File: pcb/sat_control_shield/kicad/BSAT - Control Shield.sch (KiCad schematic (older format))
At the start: 11 parts, among them P1 POWER, U1 ARDUINO_NANO_V3.0, U2 74HC4052E

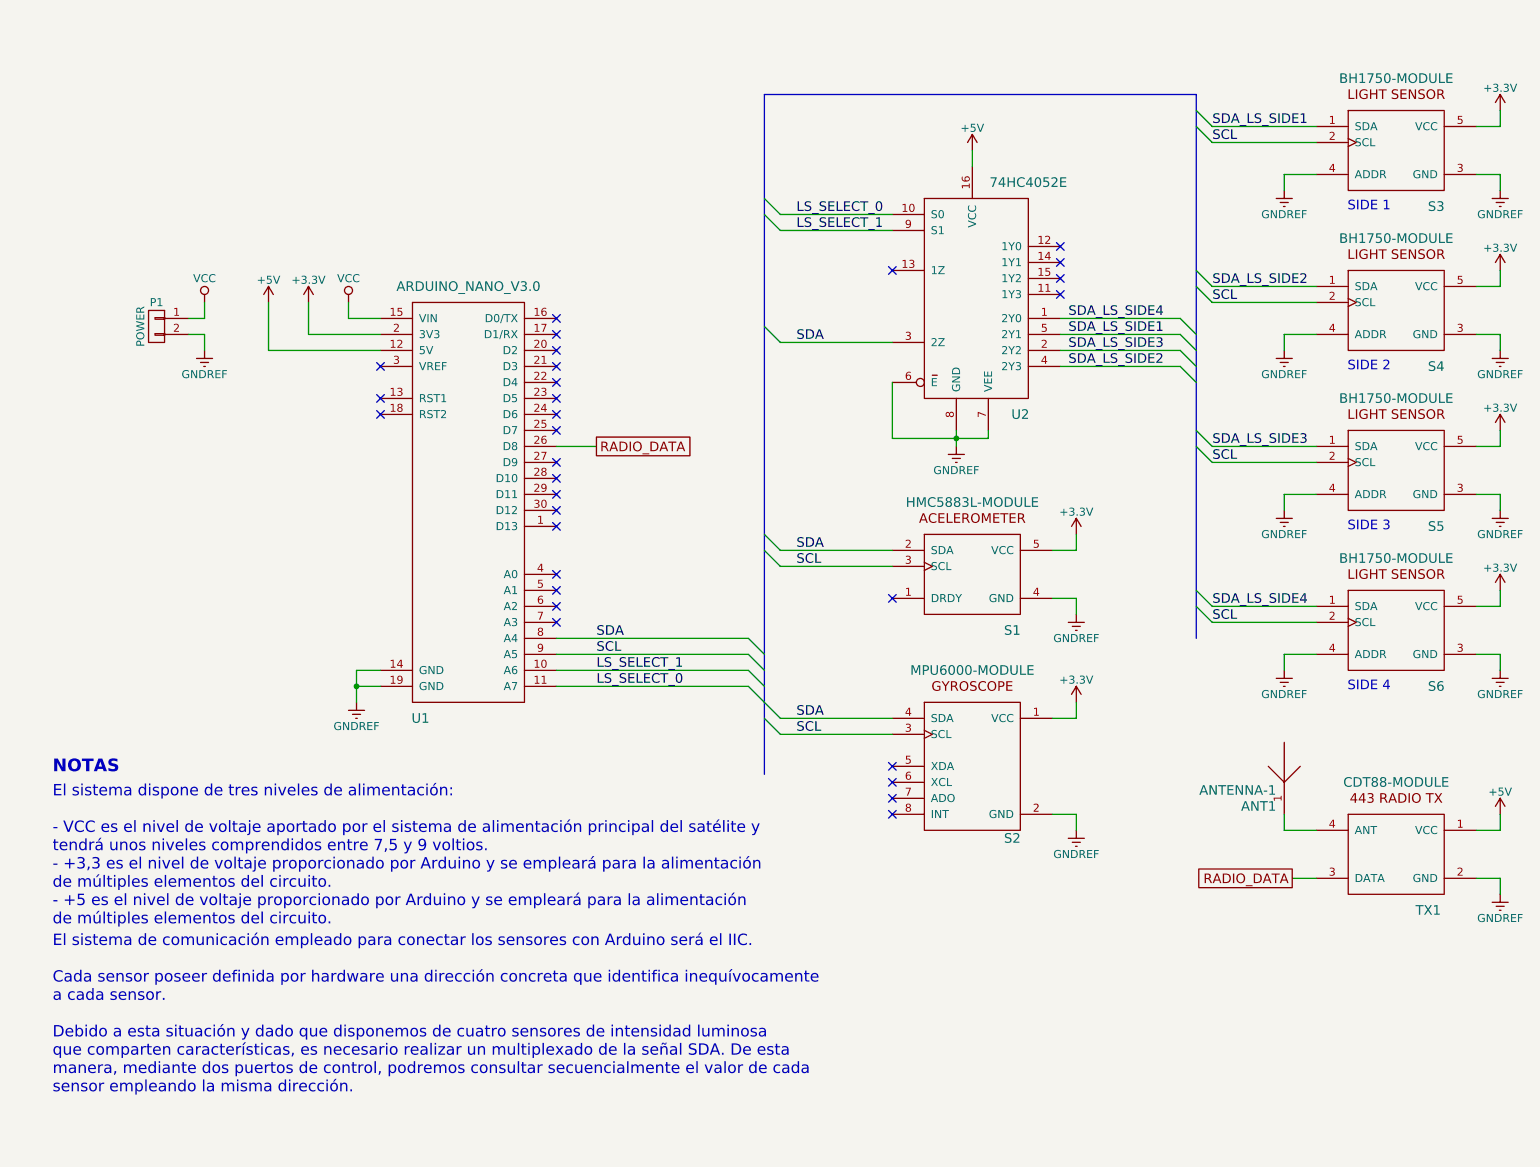
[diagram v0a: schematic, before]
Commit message: feat(control-shield): Sensor de temperatura HTU21D añadido.
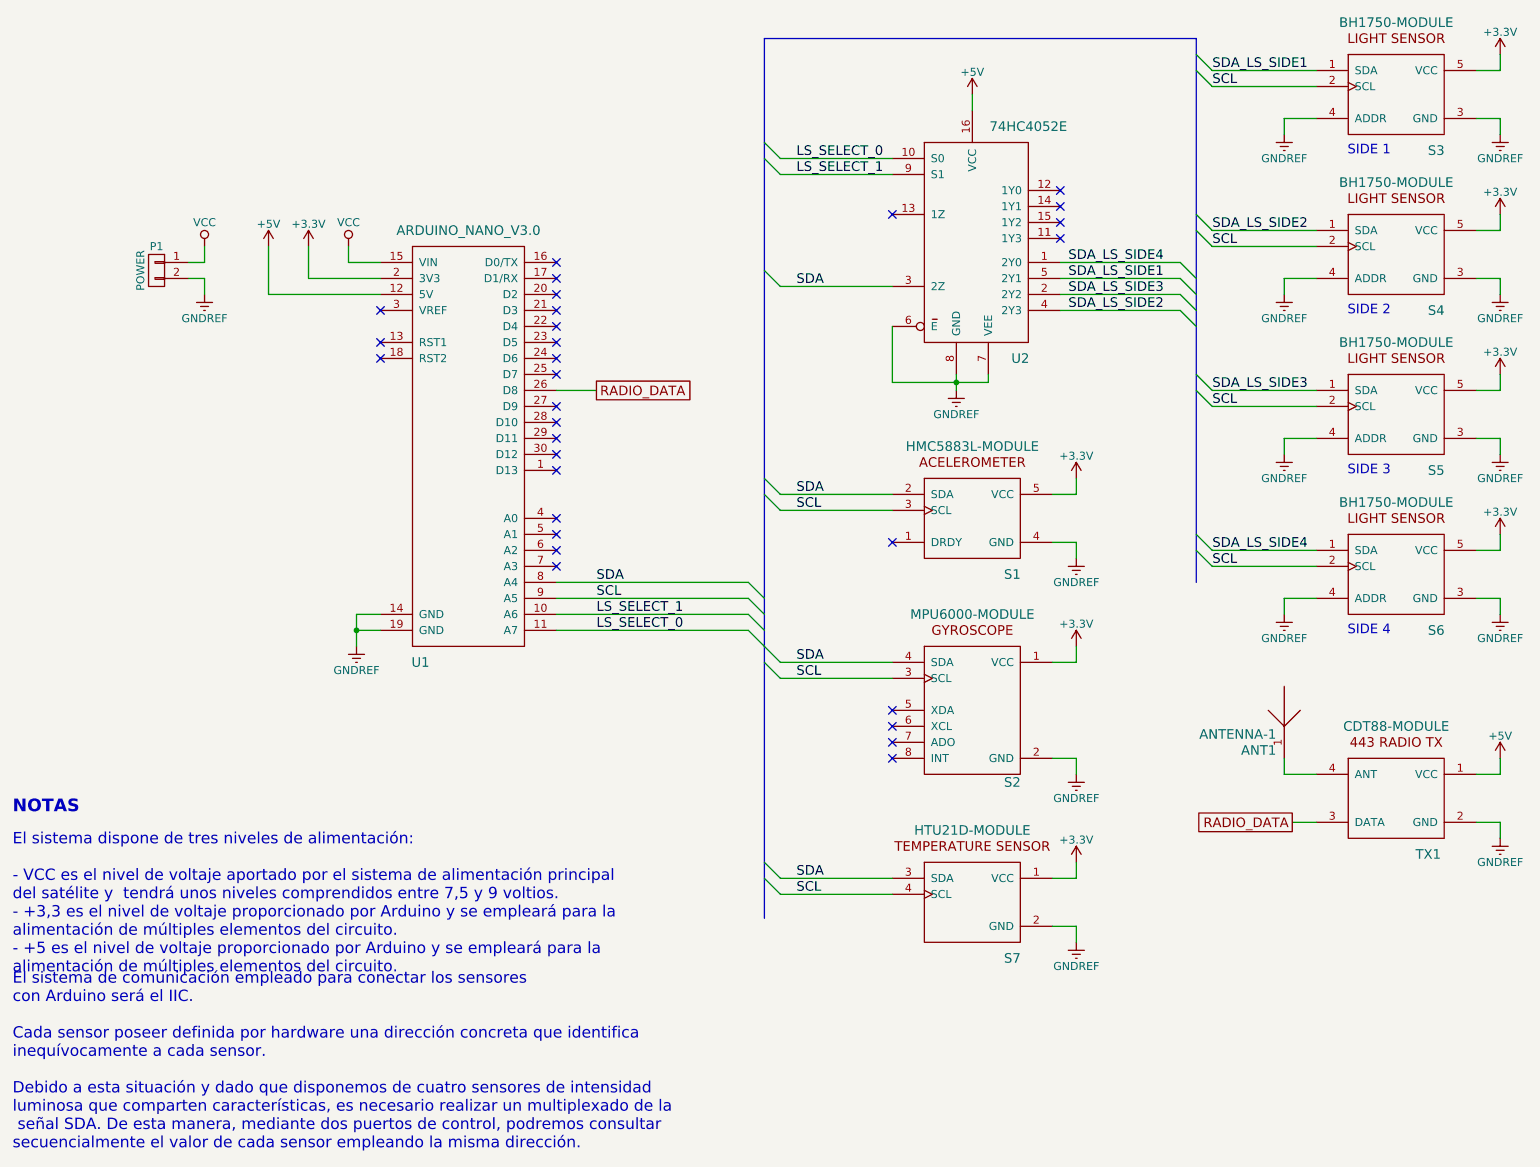
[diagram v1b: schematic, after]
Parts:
- added S7: HTU21D-MODULE, boscoverysat:HTU21D-MODULE, symbol HTU21D-MODULE
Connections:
- net +3V3: now also S7.1 (VCC)
- net GNDREF: now also S7.2 (GND)
- net SCL: now also S7.4 (SCL)
- net SDA: now also S7.3 (SDA)
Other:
- note added: "El sistema de comunicación empleado para conectar los sensores \ncon Arduino será el IIC.\n\nCada sensor poseer definida por hardware una dirección concreta que identifica\ninequívocamente a cada sensor.\n\nDebido a esta situación y dado que disponemos de cuatro sensores de intensidad\nluminosa que comparten características, es necesario realizar un multiplexado de la\n señal SDA. De esta manera,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"
- note added: "El sistema dispone de tres niveles de alimentación:\n\n- VCC es el nivel de voltaje aportado por el sistema de alimentación principal\ndel satélite y tendrá unos niveles comprendidos entre 7,5 y 9 voltios.\n- +3,3 es el nivel de voltaje proporcionado por Arduino y se empleará para la\nalimentación de múltiples elementos del circuito.\n- +5 es el nivel de voltaje proporcionado por Arduino y se emp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"
- note removed: "El sistema de comunicación empleado para conectar los sensores con Arduino será el IIC.\n\nCada sensor poseer definida por hardware una dirección concreta que identifica inequívocamente\na cada sensor.\n\nDebido a esta situación y dado que disponemos de cuatro sensores de intensidad luminosa\nque comparten características, es necesario realizar un multiplexado de la señal SDA. De esta\nmanera, me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"
- note removed: "El sistema dispone de tres niveles de alimentación:\n\n- VCC es el nivel de voltaje aportado por el sistema de alimentación principal del satélite y \ntendrá unos niveles comprendidos entre 7,5 y 9 voltios.\n- +3,3 es el nivel de voltaje proporcionado por Arduino y se empleará para la alimentación \nde múltiples elementos del circuito.\n- +5 es el nivel de voltaje proporcionado por Arduino y se e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"
- moved on the sheet: ANT1, P1, S1, S2, S3, S4, S5, S6, TX1, U1, U2
